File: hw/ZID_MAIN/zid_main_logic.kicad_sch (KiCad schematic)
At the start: 63 parts, among them J1 Conn_01x02_Pin_2.54mm, J2 Conn_02x05_2.54mm, J3 Conn_02x05_2.54mm, J4 Conn_02x05_PINHDR_2.54mm, J5 JST SH 4, J6 Conn_02x03_Odd_Even, J7 Conn_01x03, M1 WS-RP2040-Zero, SW1 SW_Push, SW2 SW_DIP_x02, U1 74HCT161, U10 74FCT2245, U11 SST39SF010, U12 AS7C1024B-10J, U13 74FCT541C, U14 74AHCT244, U15 74FCT257T, U16 74HCT166, U17 74HCT166, U18 74LVC245, U19 74LVC125AS, U2 74FCT541C, U20 24LC32, U21 ATF1504AS-44T, U22 74AHCT1G125, U23 74HCT175, U3 74FCT541C, U4 MIC2775, U6 Z80 C20MHz-PLCC, U7 ATF1508AS, U8 74FCT2245, U9 74FCT2245

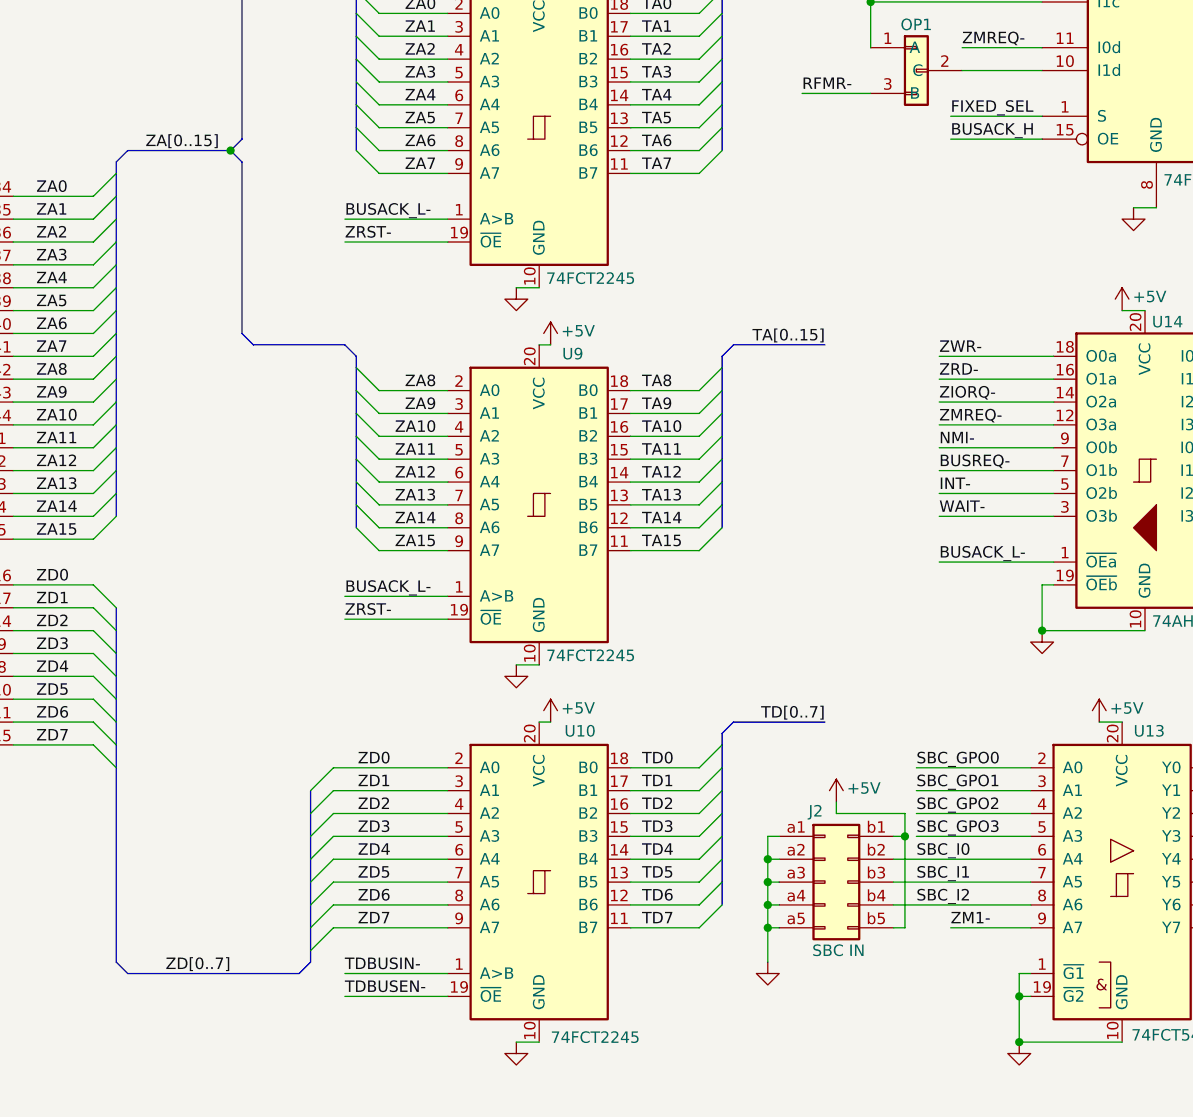
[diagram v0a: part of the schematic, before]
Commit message: Address pull-ups, small updates.
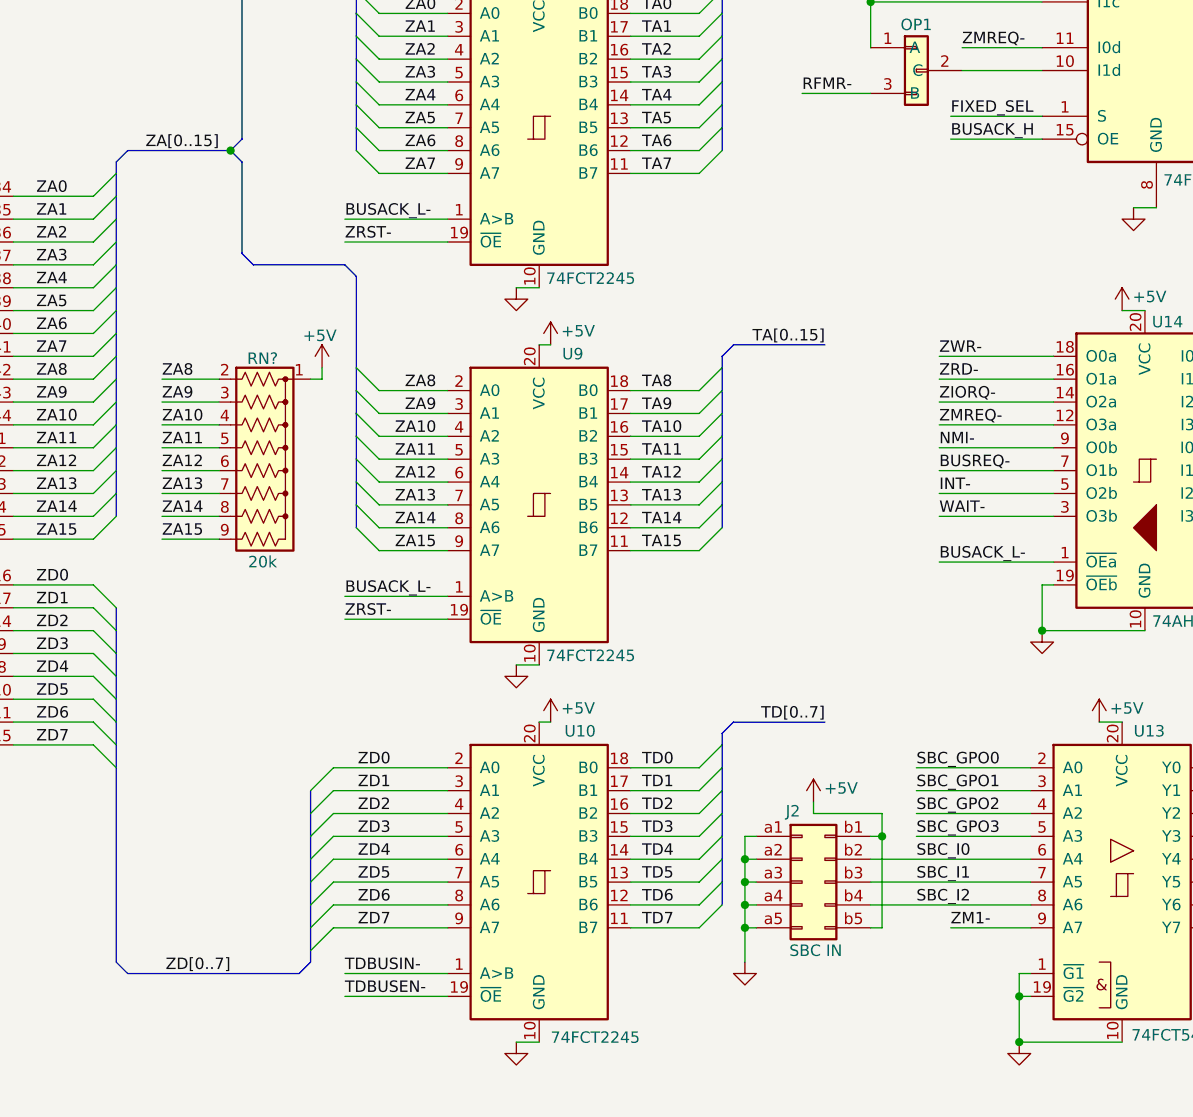
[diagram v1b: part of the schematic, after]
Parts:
- added RN?: 20k, Resistor_THT:R_Array_SIP9, symbol Device:R_Network08_US
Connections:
- net +5V: now also RN?.1 (common)
- net ZA10: now also RN?.4 (R3)
- net ZA11: now also RN?.5 (R4)
- net ZA12: now also RN?.6 (R5)
- net ZA13: now also RN?.7 (R6)
- net ZA14: now also RN?.8 (R7)
- net ZA15: now also RN?.9 (R8)
- net ZA8: now also RN?.2 (R1)
- net ZA9: now also RN?.3 (R2)
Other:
- moved on the sheet: J2

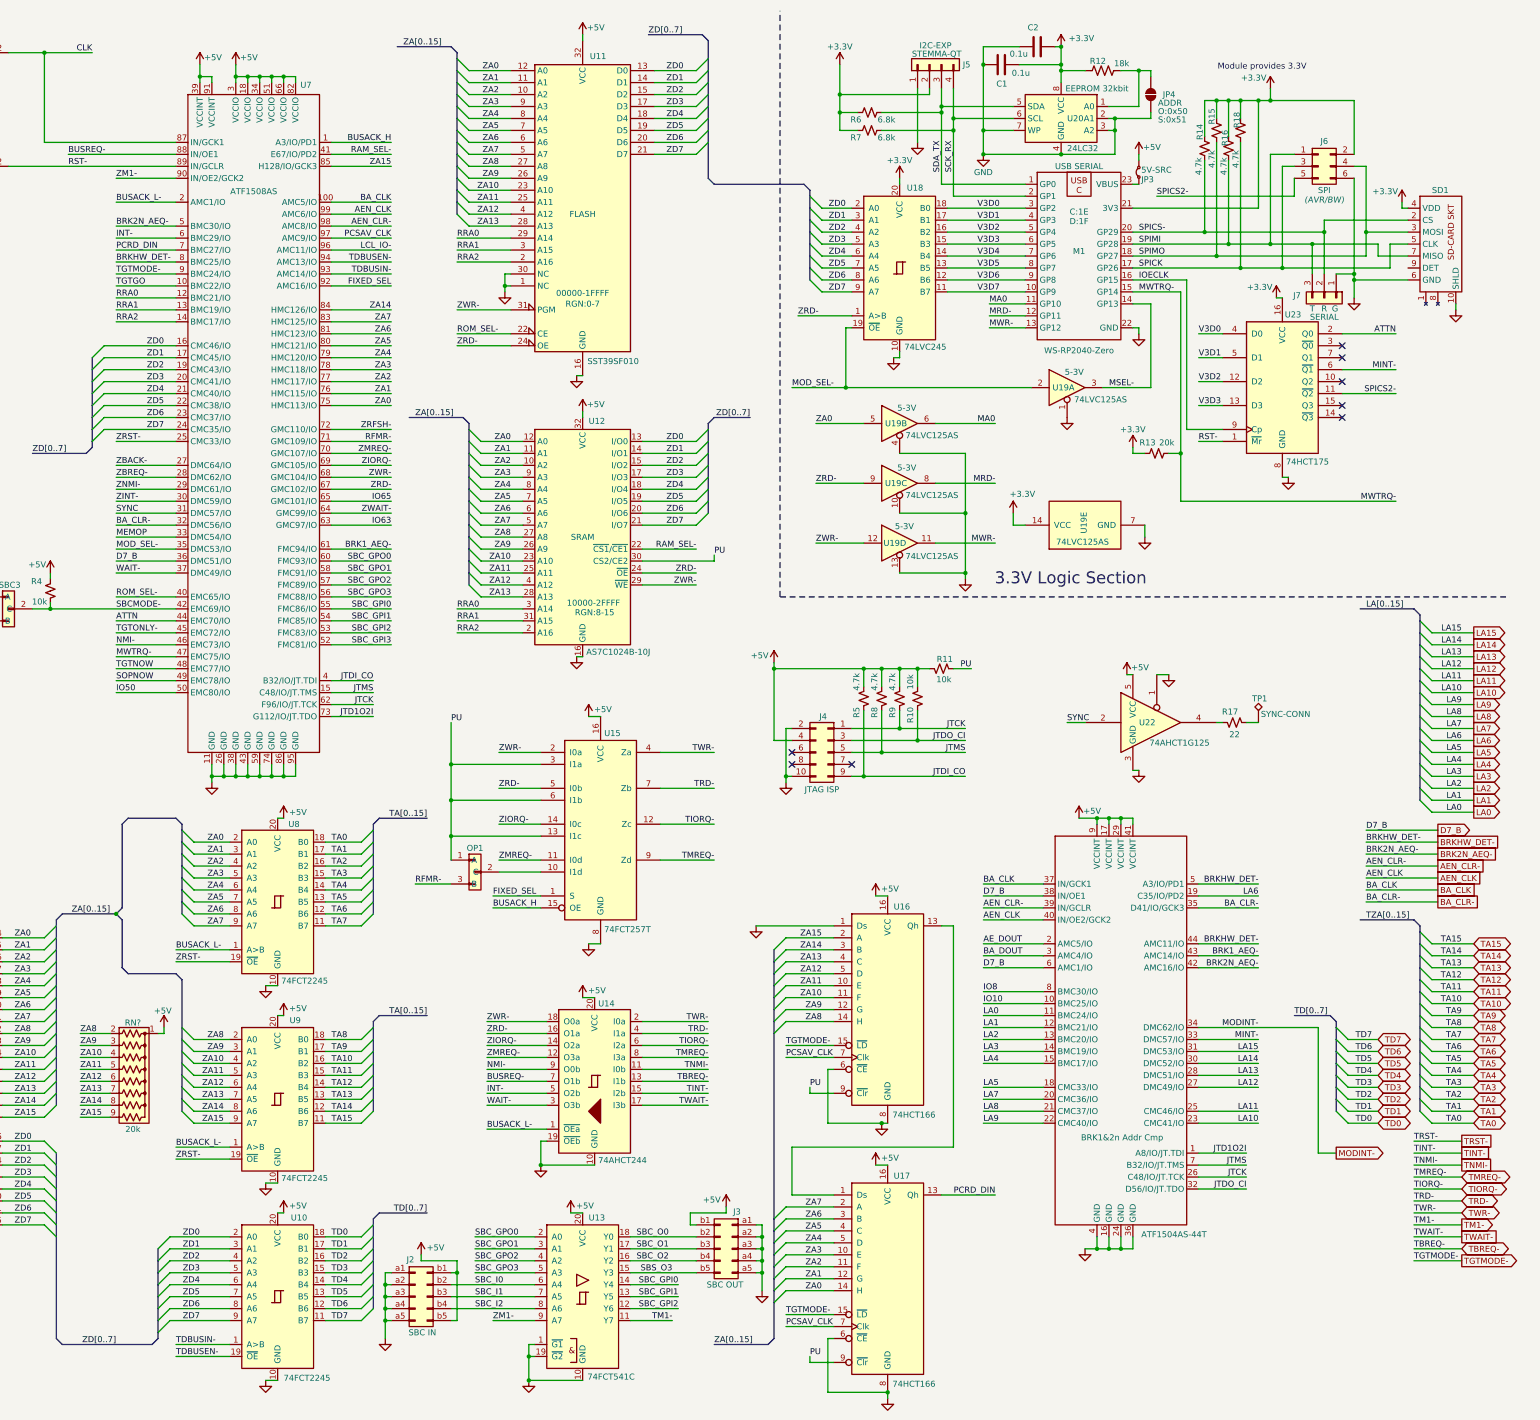
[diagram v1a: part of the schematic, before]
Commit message: Add TP for open CPLD pins
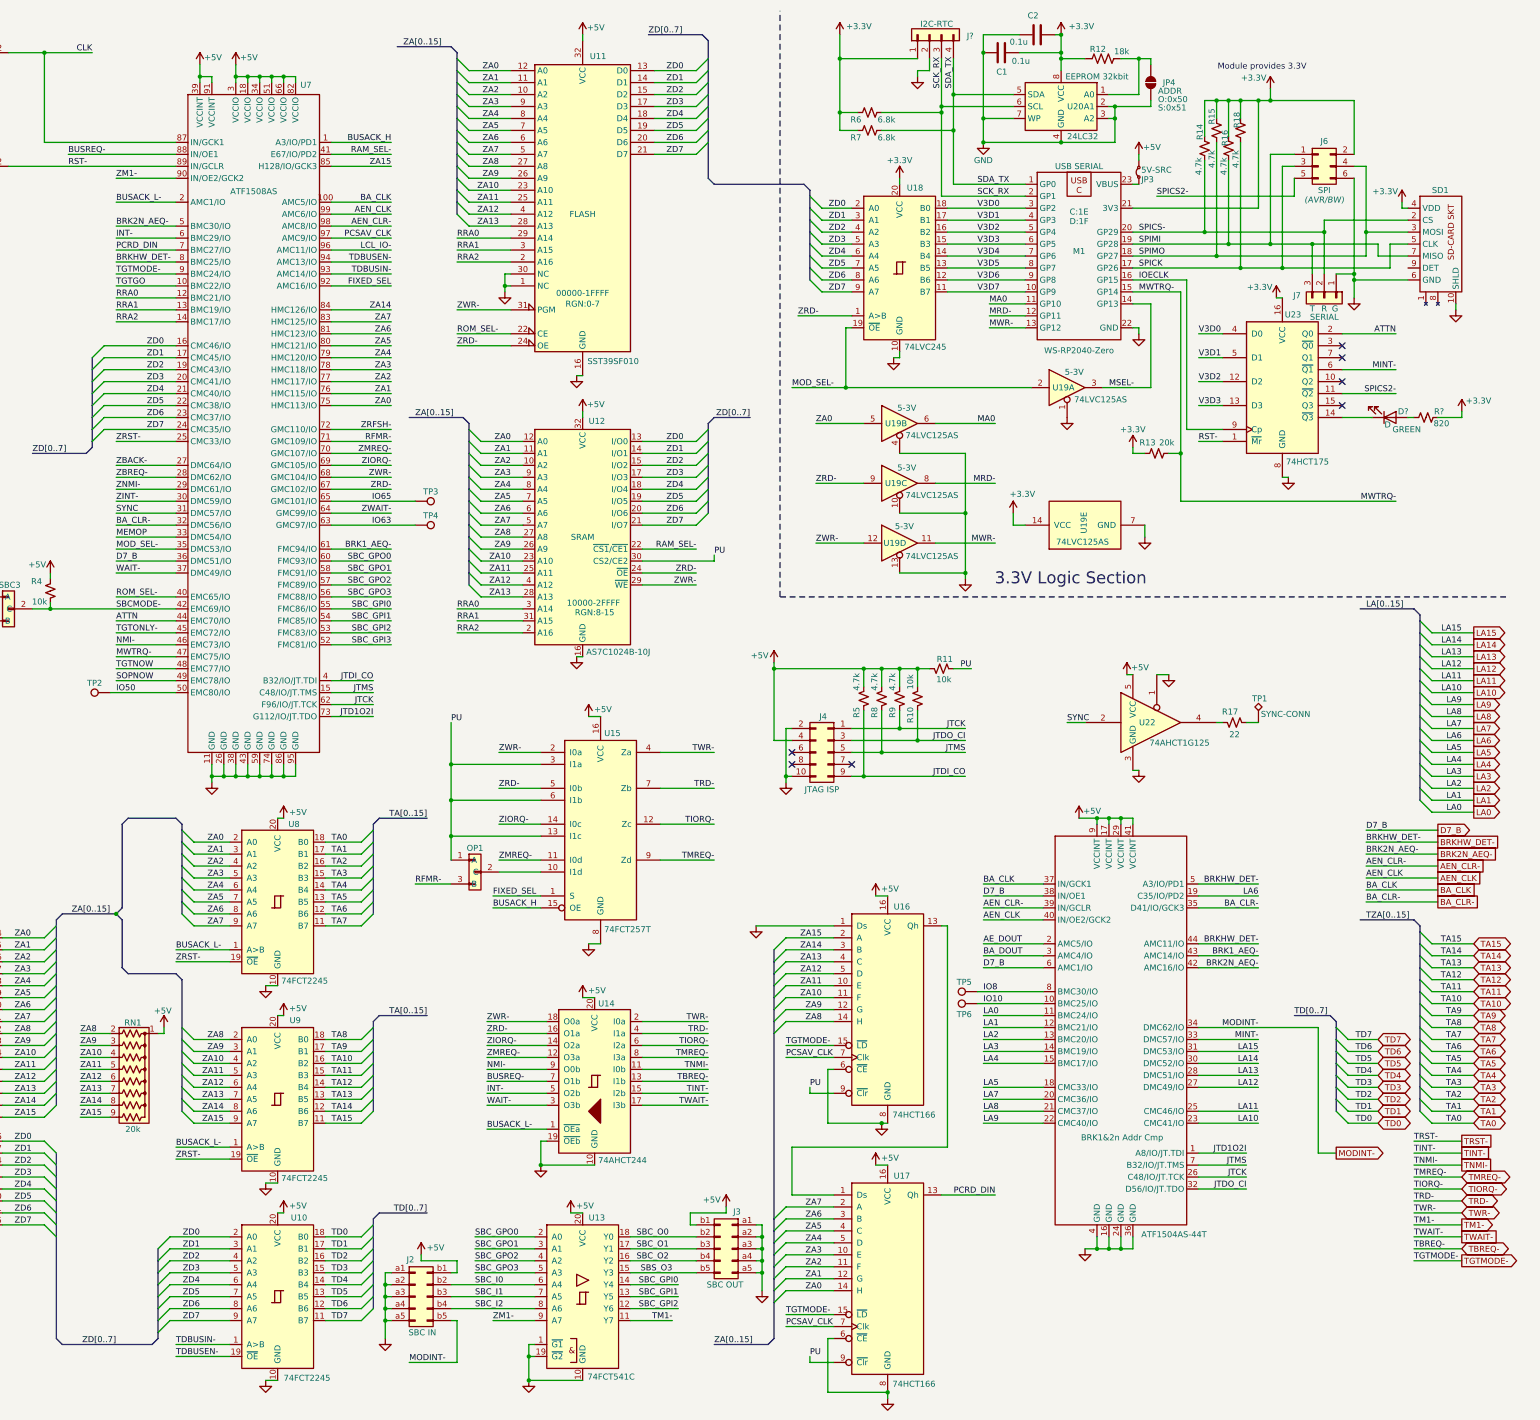
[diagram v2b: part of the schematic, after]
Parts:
- removed J5: JST SH 4, symbol Connector_Generic:Conn_01x04
- added D?: LED RED, LED_THT:LED_D3.0mm, symbol Device:LED
- added J?: HDR 1x04 Socket, Connector_PinSocket_2.54mm:PinSocket_1x04_P2.54mm_Vertical, symbol Connector_Generic:Conn_01x04
- added R?: 820, Resistor_SMD:R_0805_2012Metric, symbol Device:R_Small_US
- added TP2, TP3, TP4, TP5, TP6: TestPoint, symbol Connector:TestPoint
- gave numbers to parts that had none: 1
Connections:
- net +3.3V: now also J?.1 (Pin_1), R?.2
- net +5V: no longer J2.b5 (Pin_b5)
- net GND: now also J?.2 (Pin_2)
- net IO10: now also TP6.1
- net IO50: now also TP2.1
- net IO63: now also TP4.1
- net IO65: now also TP3.1
- net IO8: now also TP5.1
- net MODINT-: now also J2.b5 (Pin_b5)
- net SCK_RX: now also R6.1, J?.3 (Pin_3); no longer R7.1
- net SDA_TX: now also R7.1, J?.4 (Pin_4); no longer R6.1
- net at U23.14 (~{Q3}): now also D?.1 (K)
- new net: D?.2 (A), R?.1
- no-connect marks 14 -> 13
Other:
- moved on the sheet: C1, C2, JP4, R12, U20

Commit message: 8 output bits on RP. 10k PU for most. TVS.
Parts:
- removed D?: LED RED, LED_THT:LED_D3.0mm, symbol Device:LED
- removed U23: 74HCT175, symbol 74xx:74LS175
- added D5, D6, D7, D8, D9: LED RED, LED_THT:LED_D3.0mm, symbol Device:LED
- added R32, R33, R35, R36: 820, Resistor_SMD:R_0805_2012Metric, symbol Device:R_Small_US
- added U23: 74LVC273, symbol AES_Library:74273-AES
- added U25: 74LVC2G04, Package_TO_SOT_SMD:SOT-23-6, symbol AES_Library:74LVC2G04-AES
- added U26: 74LVC2G04-AES, Package_TO_SOT_SMD:SOT-23-6, symbol AES_Library:74LVC2G04-AES
- R13, R2, R3: value 20k -> 10k
- gave numbers to parts that had none: 2
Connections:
- net +3.3V: now also R32.2, R33.2, R35.2, R36.2, U23.20 (VCC), U25.5 (VCC)
- net ATTN: now also U23.2 (Q0)
- net GND: now also U23.10 (GND), U25.2 (GND)
- net IOECLK: now also U23.11 (Cp)
- net MINT-: now also U25.6
- net RST-: now also U23.1 (~{Mr})
- net SPICS2-: now also U26.4
- net V3D0: now also U23.3 (D0)
- net V3D1: now also U23.4 (D1)
- net V3D2: now also U23.7 (D2)
- net V3D3: now also U23.8 (D3)
- net V3D4: now also U23.13 (D4)
- net V3D5: now also U23.14 (D5)
- net V3D6: now also U23.17 (D6)
- net V3D7: now also U23.18 (D7)
- net at R34.1: now also D7.1 (K)
- net SBS_O3 renamed SBC_O3
- new net: U23.5 (Q1), U25.1
- new net: D5.1 (K), R32.1
- new net: D5.2 (A), U23.12 (Q4)
- new net: D8.1 (K), R35.1
- new net: D8.2 (A), U23.15 (Q5)
- new net: D7.2 (A), U23.9 (Q3)
- new net: U23.6 (Q2), U26.3
- new net: D9.1 (K), U23.19 (Q7)
- new net: D9.2 (A), R36.1
- new net: D6.1 (K), R33.1
- new net: D6.2 (A), U23.16 (Q6)
- no-connect marks 13 -> 9
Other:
- company: SilkyDESIGN -> SilkyDESIGN / CMOS1
- moved on the sheet: R34
